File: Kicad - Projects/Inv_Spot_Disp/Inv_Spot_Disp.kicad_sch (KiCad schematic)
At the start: 36 parts, among them J1 PWM, J2 Power_Supply, J3 Current_Sense, J4 Rail_Sense, J5 Softstart, J6 Rail_Sense, SW1 SW_MEC_5E, SW2 SW_MEC_5E, SW3 SW_MEC_5E, SW4 SW_MEC_5E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

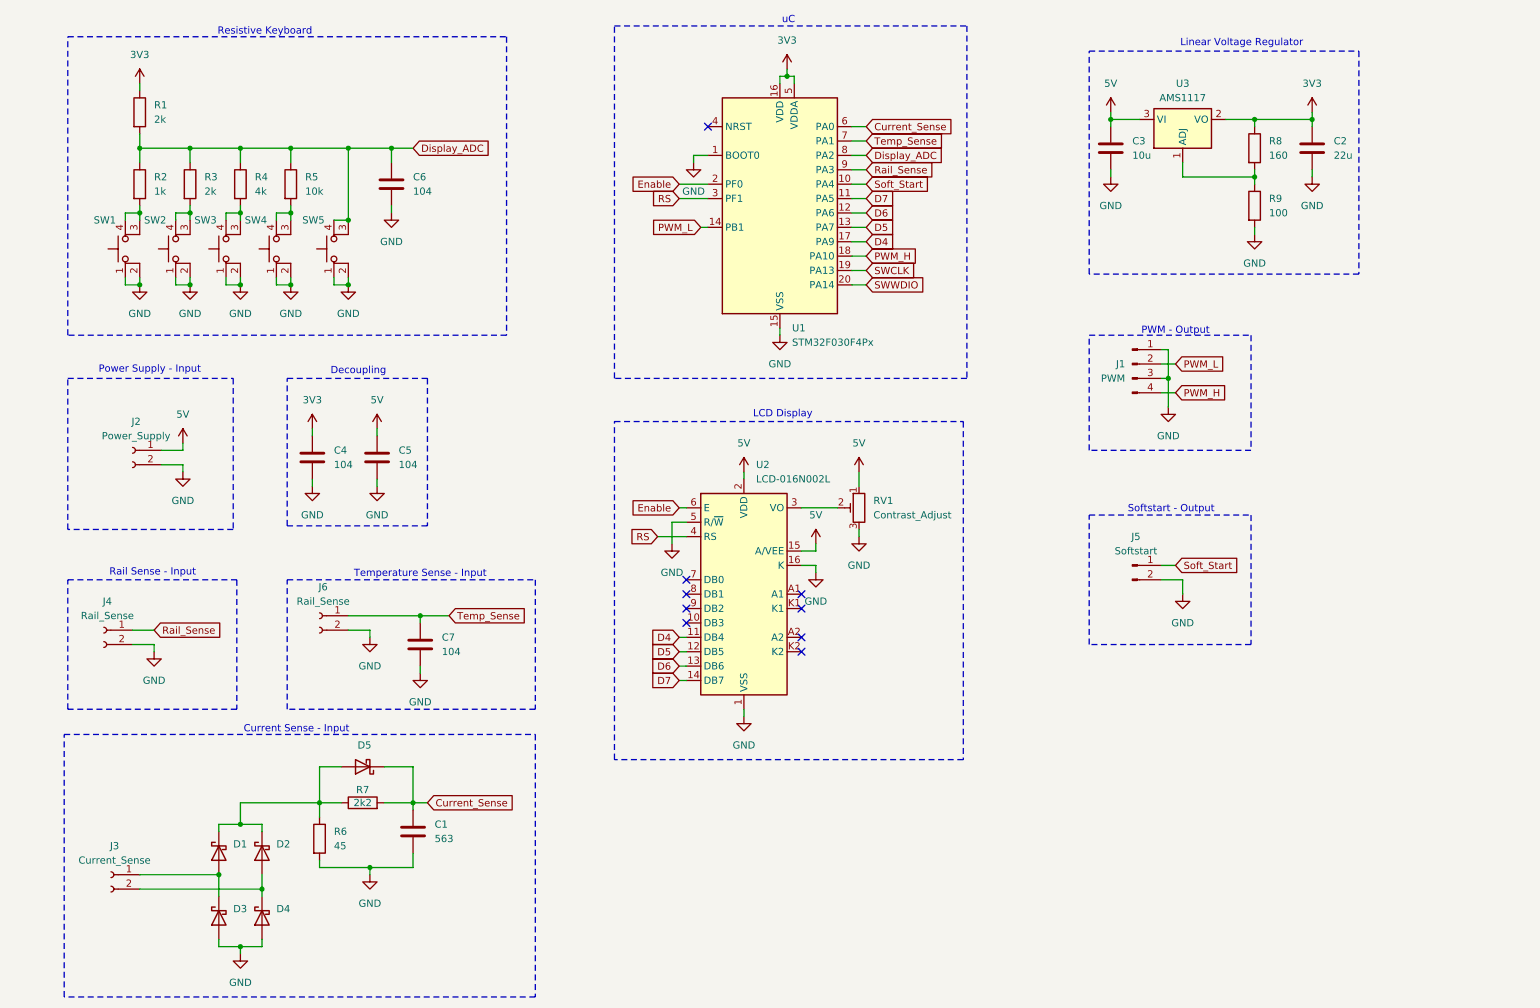
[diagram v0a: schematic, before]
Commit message: Adicionando Fonte Auxiliar
Fonte auxiliar com topologia flyback dimencionada, falta criar o footprint do transformador, abrir o espaço na placa e finalizar o roteamento dos componentes
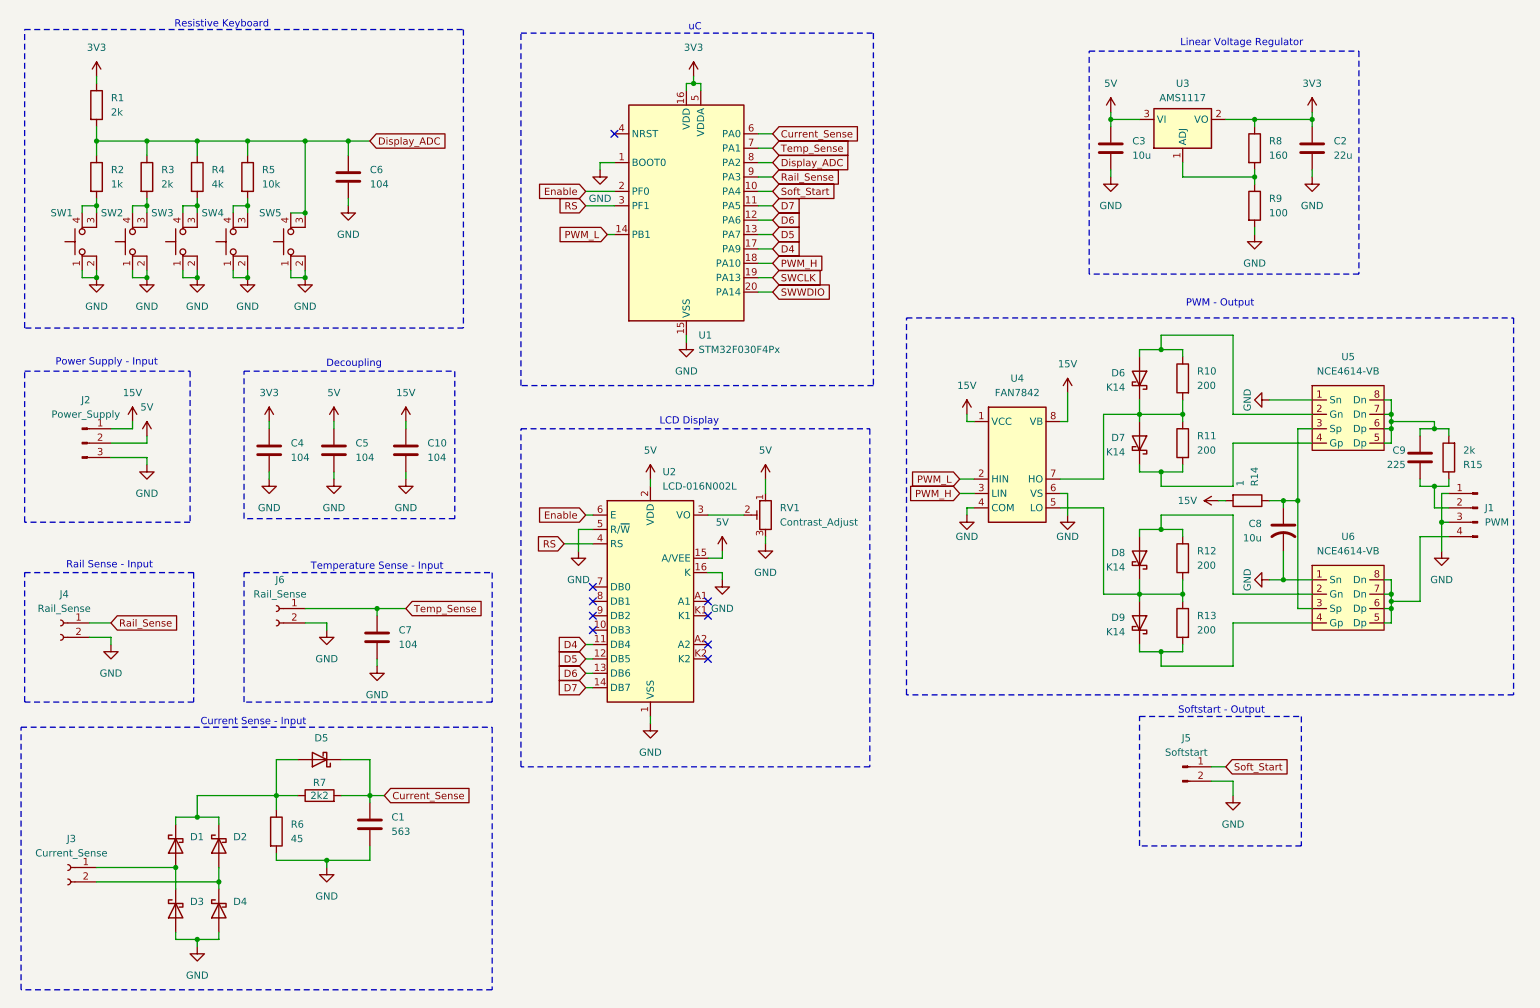
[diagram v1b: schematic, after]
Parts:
- removed J2: Power_Supply, Connector_Hirose:Hirose_DF13-02P-1.25DSA_1x02_P1.25mm_Vertical, symbol Connector:Conn_01x02_Socket
- added C10: 104, Capacitor_SMD:C_1206_3216Metric_Pad1.33x1.80mm_HandSolder, symbol Device:C
- added C8: 10u, Capacitor_THT:C_Radial_D6.3mm_H5.0mm_P2.50mm, symbol Device:C_US
- added C9: 225, Capacitor_SMD:C_1206_3216Metric_Pad1.33x1.80mm_HandSolder, symbol Device:C
- added D6, D7, D8, D9: K14, Diode_SMD:D_SOD-123F, symbol Device:D_Schottky
- added J2: Power_Supply, Connector_PinHeader_2.00mm:PinHeader_1x03_P2.00mm_Vertical, symbol Connector:Conn_01x03_Pin
- added R10, R11, R12, R13: 200, Resistor_SMD:R_1206_3216Metric_Pad1.30x1.75mm_HandSolder, symbol Device:R
- added R14: 1, Resistor_SMD:R_1206_3216Metric_Pad1.30x1.75mm_HandSolder, symbol Device:R
- added R15: 2k, Resistor_SMD:R_1206_3216Metric_Pad1.30x1.75mm_HandSolder, symbol Device:R
- added U4: FAN7842, Package_SO:SOIC-8_3.9x4.9mm_P1.27mm, symbol Driver_FET:FAN7842
- added U5, U6: NCE4614-VB, Package_SO:TSSOP-8_3x3mm_P0.65mm, symbol drivers_sym:NCE_4614-SOP8
- J1: footprint Connector_JST:JST_1x04P_P3.96mm_Vertical -> Connector_PinHeader_2.00mm:PinHeader_1x04_P2.00mm_Vertical
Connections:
- net 5V: now also J2.2 (Pin_2)
- net GND: now also C10.2, C8.2, J2.3 (Pin_3), U4.4 (COM), U4.6 (VS), U5.1 (Sn), U6.1 (Sn)
- net PWM_H: now also U4.3 (LIN); no longer J1.4 (Pin_4)
- net PWM_L: now also U4.2 (HIN); no longer J1.2 (Pin_2)
- new net: D6.2 (A), R10.1, U5.2 (Gn)
- new net: D6.1 (K), D7.2 (A), R10.2, R11.1, U4.7 (HO)
- new net: D9.1 (K), R13.2, U6.4 (Gp)
- new net: D8.1 (K), D9.2 (A), R12.2, R13.1, U4.5 (LO)
- new net: C8.1, R14.1, U5.3 (Sp), U6.3 (Sp)
- new net: D7.1 (K), R11.2, U5.4 (Gp)
- new net: C9.2, J1.2 (Pin_2), R15.1
- new net: J1.4 (Pin_4), U6.5 (Dp), U6.6 (Dp), U6.7 (Dn), U6.8 (Dn)
- new net: C9.1, R15.2, U5.5 (Dp), U5.6 (Dp), U5.7 (Dn), U5.8 (Dn)
- new net: D8.2 (A), R12.1, U6.2 (Gn)
- new net 15V: C10.1, J2.1 (Pin_1), R14.2, U4.1 (VCC), U4.8 (VB)
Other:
- moved on the sheet: C1, C4, C5, C6, C7, D1, D2, D3, D4, D5, J3, J4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

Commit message: Ajustes de Esquemático - Display
Ajustes no esquemático da placa de display:
 - Removido trigger do teclado resistivo
 - Melhora do circuito de detecção de corrente
 - Simplificação do circuito de drive - falta adicionar filtro RC antes da saída

À fazer:
 - Implementar Opto para leitura digital do gatilho de disparo
 - Trocar footprints para Pin Header/SMD
 - Roteamento da PCB
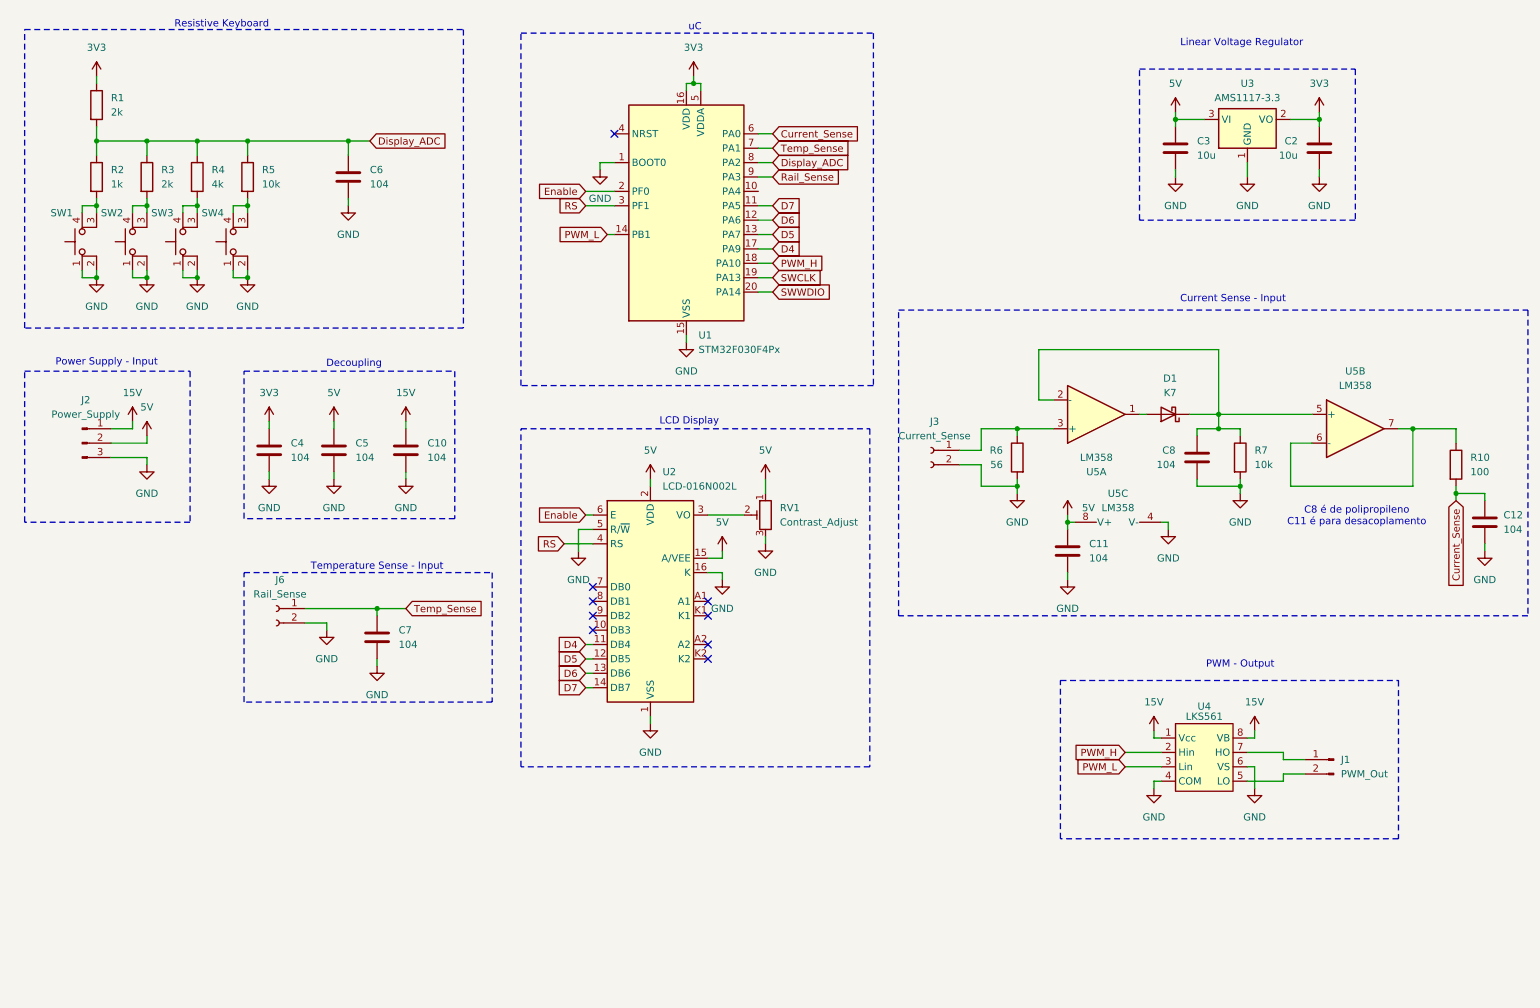
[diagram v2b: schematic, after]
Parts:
- removed C1: 563, symbol Device:C
- removed C8: 10u, Capacitor_THT:C_Radial_D6.3mm_H5.0mm_P2.50mm, symbol Device:C_US
- removed C9: 225, Capacitor_SMD:C_1206_3216Metric_Pad1.33x1.80mm_HandSolder, symbol Device:C
- removed D2, D3, D4, D5: D_Schottky, Diode_SMD:D_SOD-123F, symbol Device:D_Schottky
- removed D6, D7, D8, D9: K14, Diode_SMD:D_SOD-123F, symbol Device:D_Schottky
- removed J1: PWM, Connector_PinHeader_2.00mm:PinHeader_1x04_P2.00mm_Vertical, symbol Connector:Conn_01x04_Pin
- removed J4: Rail_Sense, Connector_Hirose:Hirose_DF13-02P-1.25DSA_1x02_P1.25mm_Vertical, symbol Connector:Conn_01x02_Socket
- removed J5: Softstart, Connector_Hirose:Hirose_DF13-02P-1.25DSA_1x02_P1.25mm_Vertical, symbol Connector:Conn_01x02_Pin
- removed R11, R12, R13: 200, Resistor_SMD:R_1206_3216Metric_Pad1.30x1.75mm_HandSolder, symbol Device:R
- removed R14: 1, Resistor_SMD:R_1206_3216Metric_Pad1.30x1.75mm_HandSolder, symbol Device:R
- removed R15: 2k, Resistor_SMD:R_1206_3216Metric_Pad1.30x1.75mm_HandSolder, symbol Device:R
- removed R8: 160, symbol Device:R
- removed R9: 100, symbol Device:R
- removed SW5: SW_MEC_5E, Button_Switch_THT:Tactile_Switch_W6mm, symbol Switch:SW_MEC_5E
- removed U3: AMS1117, Package_TO_SOT_SMD:SOT-223-3_TabPin2, symbol Regulator_Linear:AMS1117
- removed U4: FAN7842, Package_SO:SOIC-8_3.9x4.9mm_P1.27mm, symbol Driver_FET:FAN7842
- removed U5, U6: NCE4614-VB, Package_SO:TSSOP-8_3x3mm_P0.65mm, symbol drivers_sym:NCE_4614-SOP8
- added C11, C12: 104, Capacitor_SMD:C_1206_3216Metric_Pad1.33x1.80mm_HandSolder, symbol Device:C
- added C8: 104, Capacitor_THT:C_Rect_L10.0mm_W3.0mm_P7.50mm_MKS4, symbol Device:C
- added J1: PWM_Out, Connector_PinHeader_2.00mm:PinHeader_1x02_P2.00mm_Vertical, symbol Connector:Conn_01x02_Pin
- added U3: AMS1117-3.3, Package_TO_SOT_SMD:SOT-223-3_TabPin2, symbol Regulator_Linear:AMS1117-3.3
- added U4: LKS561, Package_SO:SSOP-8_3.9x5.05mm_P1.27mm, symbol Custom_ICs:LKS561
- added U5: LM358, symbol Amplifier_Operational:LM358
- C2: value 22u -> 10u
- D1: value D_Schottky -> K7; footprint Diode_SMD:D_SOD-123F -> Diode_SMD:D_SOD-323_HandSoldering
- R10: value 200 -> 100
- R6: value 45 -> 56; footprint (none) -> Resistor_SMD:R_1206_3216Metric_Pad1.30x1.75mm_HandSolder
- R7: value 2k2 -> 10k; footprint (none) -> Resistor_SMD:R_1206_3216Metric_Pad1.30x1.75mm_HandSolder
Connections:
- net 15V: now also U4.1 (Vcc), U4.8 (VB)
- net 3V3: now also U3.2 (VO)
- net 5V: now also C11.1, U3.3 (VI), U5.8 (V+)
- net Current_Sense: now also R10.2, C12.1; no longer R7.2
- net GND: now also J3.2 (Pin_2), R7.2, C11.2, C12.2, C8.2, U3.1 (GND), U4.4 (COM), U4.6 (VS), U5.4 (V-)
- net PWM_H: now also U4.2 (Hin)
- net PWM_L: now also U4.3 (Lin)
- net at D1.1 (K), R7.1: now also C8.1, U5.2 (-), U5.5 (+); no longer R6.1
- net at R10.1: now also U5.6 (-), U5.7
- net at J3.1 (Pin_1): now also R6.1, U5.3 (+); no longer D1.2 (A)
- net Soft_Start: no longer names the net of U1.10 (PA4)
- new net: D1.2 (A), U5.1
- new net: J1.1 (Pin_1), U4.7 (HO)
- new net: J1.2 (Pin_2), U4.5 (LO)
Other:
- note added: "C8 é de polipropileno C11 é para desacoplamento"
- note removed: "Rail Sense - Input"
- note removed: "Softstart - Output"
- moved on the sheet: C2, C3, J3

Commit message: Ajustes de Esquemático - Display
Feito:
 - Ajustes genéricos para melhor legibilidade
 - Implementado Opto para leitura do gatilho (com pull-up no lado do uC)
 - Trocados footprints das conexões para pinheader
 - Ajuste na trilha T- do IGBT superior

À fazer:
 - Trocar todos os resistores por SMD
 - Revisar com Anderson sobre topologias/conectores
 - Revisar com Anderson sobre afastamento do plano de referência da trilha "Earth" dos IGBTs inferiores
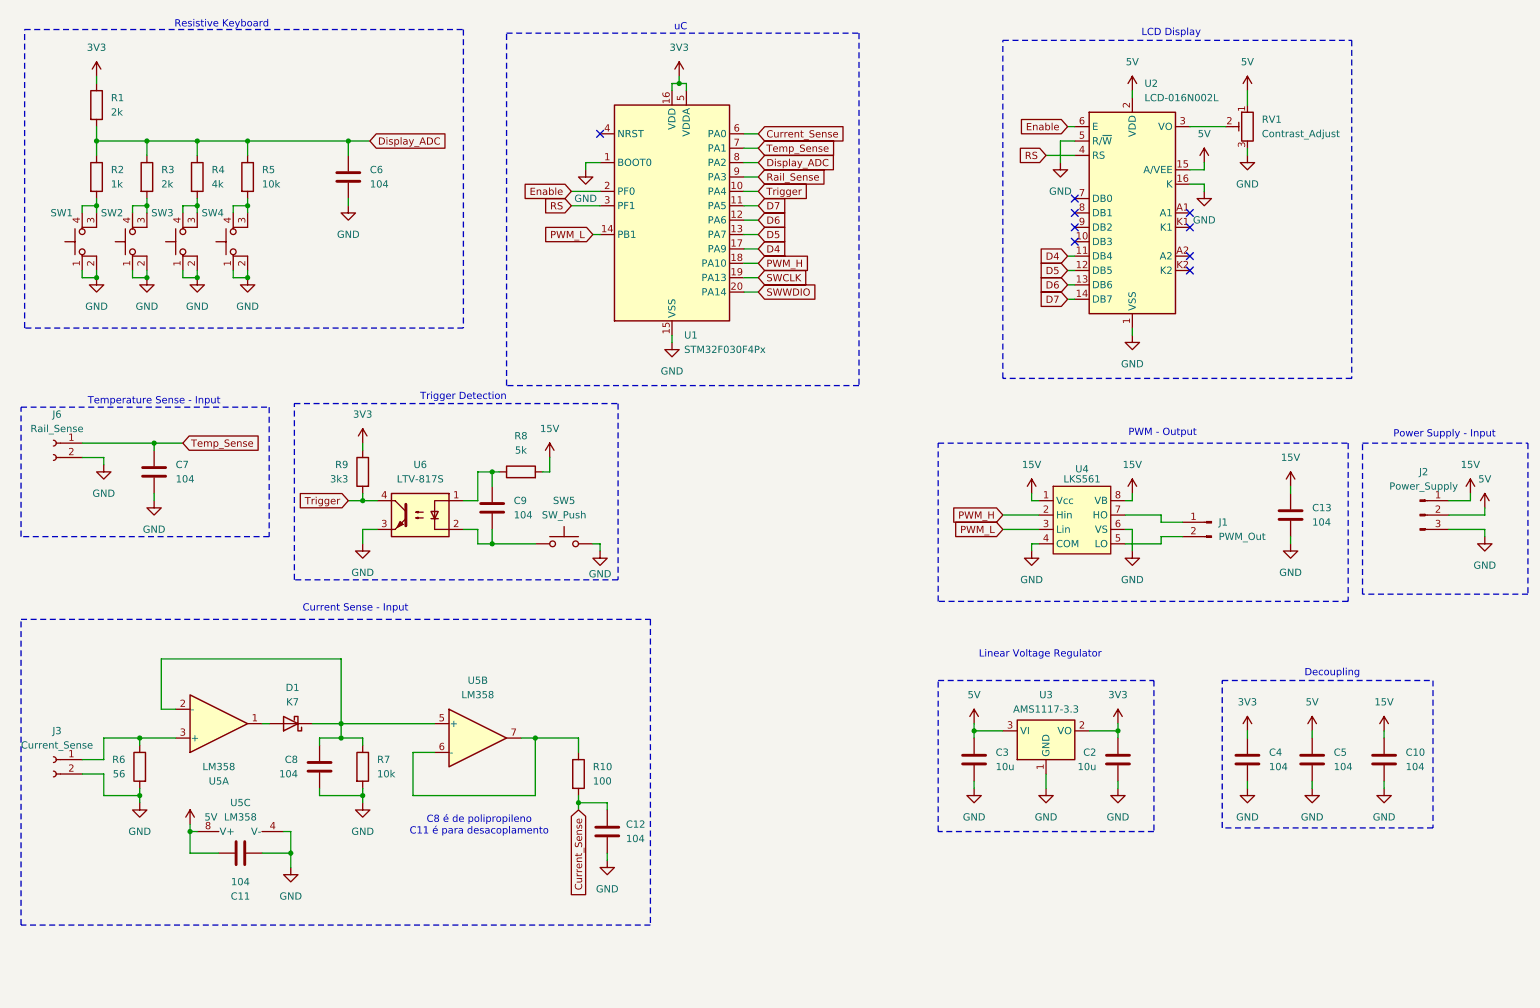
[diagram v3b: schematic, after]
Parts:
- added C13, C9: 104, Capacitor_SMD:C_1206_3216Metric_Pad1.33x1.80mm_HandSolder, symbol Device:C
- added R8: 5k, Resistor_SMD:R_1206_3216Metric_Pad1.30x1.75mm_HandSolder, symbol Device:R
- added R9: 3k3, Resistor_SMD:R_1206_3216Metric_Pad1.30x1.75mm_HandSolder, symbol Device:R
- added SW5: SW_Push, Button_Switch_THT:SW_PUSH_1P1T_6x3.5mm_H4.3_APEM_MJTP1243, symbol Switch:SW_Push
- added U6: LTV-817S, Package_DIP:SMDIP-4_W9.53mm, symbol Isolator:LTV-817S
- J3, J6: footprint Connector_Hirose:Hirose_DF13-02P-1.25DSA_1x02_P1.25mm_Vertical -> Connector_PinHeader_2.00mm:PinHeader_1x02_P2.00mm_Vertical
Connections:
- net 15V: now also C13.1, R8.2
- net 3V3: now also R9.1
- net GND: now also C13.2, SW5.2, U6.3
- net Trigger: now reaches U1.10 (PA4)
- net Trigger: now also R9.2, U6.4
- new net: C9.1, R8.1, U6.1
- new net: C9.2, SW5.1, U6.2
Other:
- note added: "Trigger Detection"
- moved on the sheet: C10, C11, C12, C2, C3, C4, C5, C7, C8, D1, J1, J2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
